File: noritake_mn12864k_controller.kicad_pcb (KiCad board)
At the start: 4 copper layers, 85 x 46.5 mm, 148 parts, among them J1 Conn_01x11, J2 USB_C_Receptacle_USB2.0, J3 TagConnect_TC2030_SWD, J4 Conn_01x18, Q1 AO3400A, Q10 2N7002, Q11 LBSS84LT1G, Q12 2N7002, Q13 TO-252, Q14 CJT04N15, Q15 2N7002, Q16 LBSS84LT1G, Q17 2N7002, Q18 S9015, Q2 AO3400A, Q3 S9015, Q4 AO3401A, Q5 AO3401A, Q6 S9015, Q7 2N7002, Q8 LBSS84LT1G, Q9 2N7002, T1 Wuerth 760390013, T2 Wuerth 760390013, T3 Wuerth 760390013, U1 SN74AVC8T245PW, U10 SRV05-4, U11 SRV05-4, U12 SRV05-4, U2 74HC14, U3 CD4051B, U4 MN12864K, U5 STM32F730R8T6, U6 NE555D, U7 74HC08, U8 SRV05-4, U9 XC6206PxxxMR

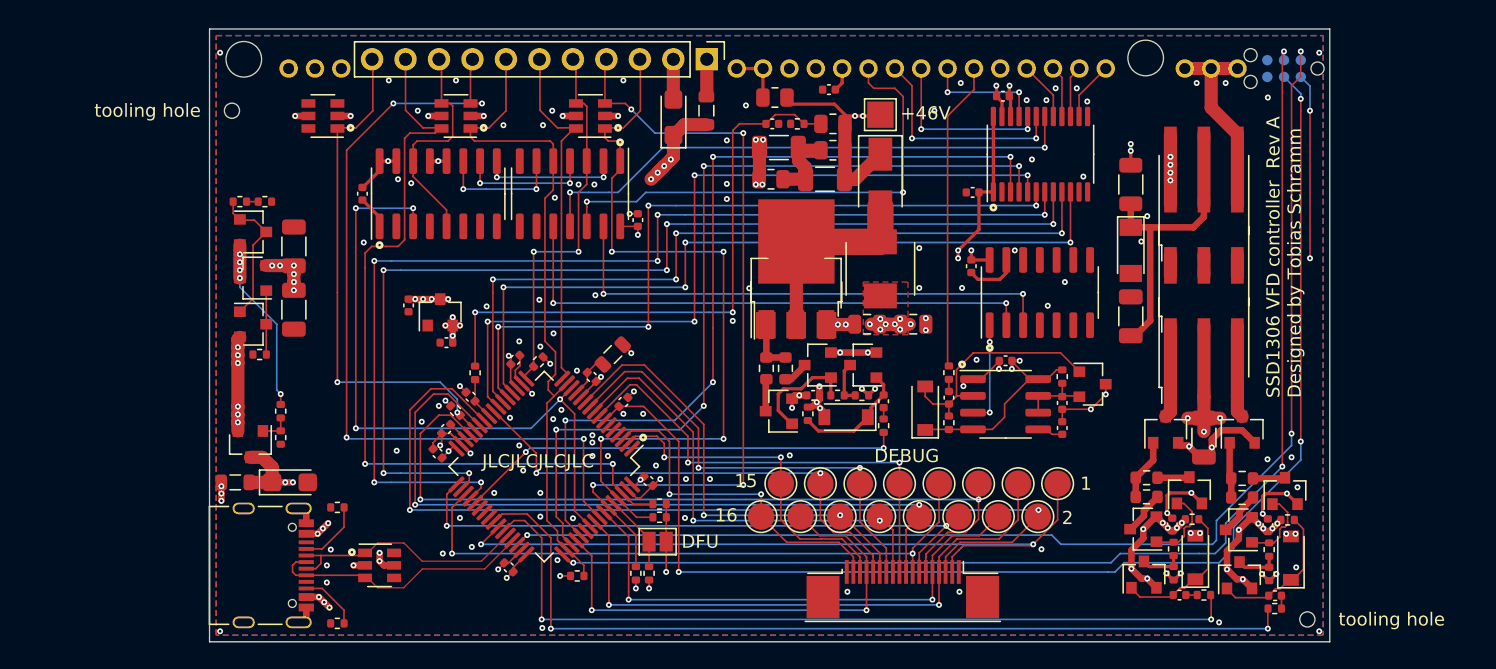
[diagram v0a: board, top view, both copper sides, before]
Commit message: Fix level shifter
Level shifter was flipped in scheatic
Pressed "y" one too many times on that thing :/
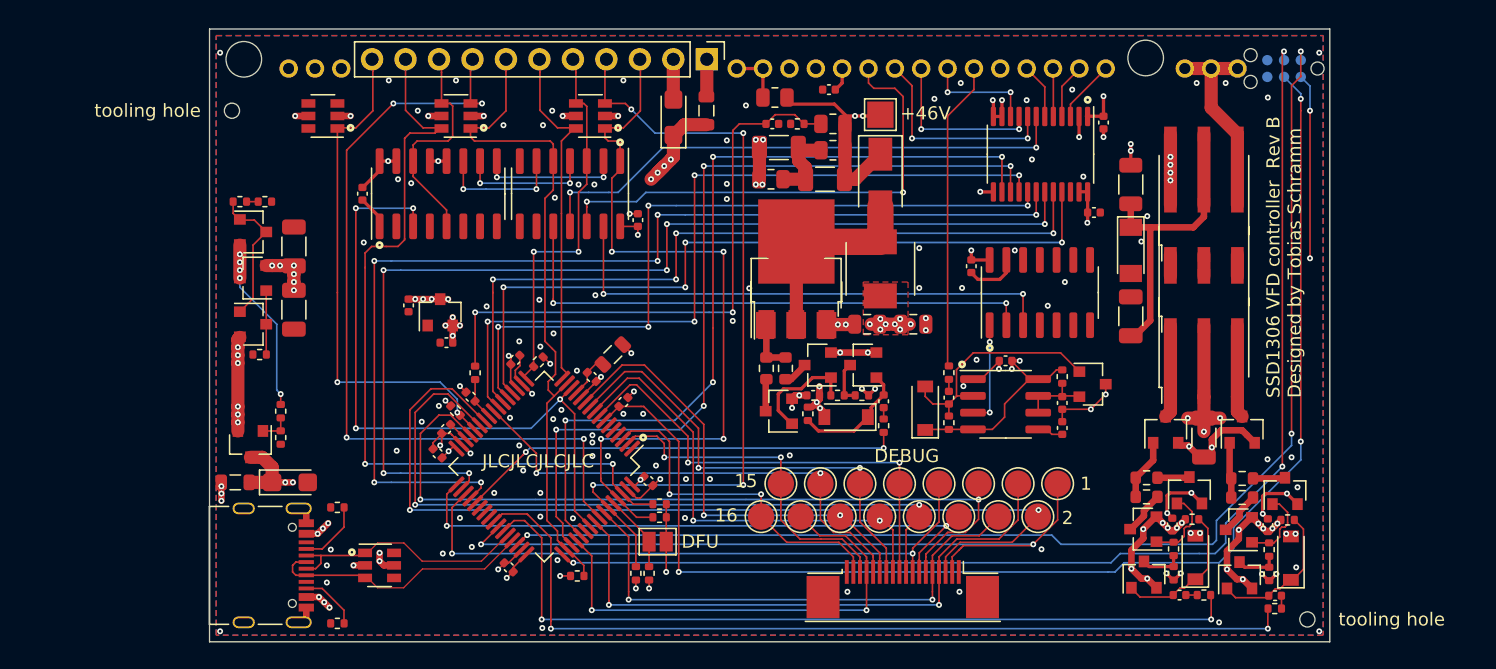
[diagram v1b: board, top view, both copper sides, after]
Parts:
- moved C5 9.33 mm to (167.1, 109.4), turned to 0 degrees
- moved C6 7.89 mm to (167.8, 102.6), turned to 90 degrees
- turned U1 to 270 degrees
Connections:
- U1 pad 1: +3V3 -> +5V
- U1 pad 10: /VFD_BLK -> Net-(U1-Pad10)
- U1 pad 14: Net-(U1-Pad14) -> /VFD_GSIN
- U1 pad 15: Net-(U1-Pad15) -> /VFD_GCLK
- U1 pad 16: Net-(U1-Pad16) -> /VFD_GLAT
- U1 pad 17: Net-(U1-Pad17) -> /VFD_GSBLK
- U1 pad 18: /VFD/sheet60B1BFBD/GBLK_IN -> /VFD_SIN
- U1 pad 19: Net-(U1-Pad19) -> /VFD_CLK
- U1 pad 20: Net-(U1-Pad20) -> /VFD_LAT
- U1 pad 21: Net-(U1-Pad21) -> /VFD_BLK
- U1 pad 23: +5V -> +3V3
- U1 pad 3: /VFD_GSIN -> Net-(U1-Pad3)
- U1 pad 4: /VFD_GCLK -> Net-(U1-Pad4)
- U1 pad 5: /VFD_GLAT -> Net-(U1-Pad5)
- U1 pad 6: /VFD_GSBLK -> Net-(U1-Pad6)
- U1 pad 7: /VFD_SIN -> /VFD/sheet60B1BFBD/GBLK_IN
- U1 pad 8: /VFD_CLK -> Net-(U1-Pad8)
- U1 pad 9: /VFD_LAT -> Net-(U1-Pad9)
- U4 pad 12: Net-(U1-Pad21) -> Net-(U1-Pad10)
- U4 pad 13: Net-(U1-Pad20) -> Net-(U1-Pad9)
- U4 pad 14: Net-(U1-Pad19) -> Net-(U1-Pad8)
- U4 pad 6: Net-(U1-Pad14) -> Net-(U1-Pad3)
- U4 pad 7: Net-(U1-Pad15) -> Net-(U1-Pad4)
- U4 pad 8: Net-(U1-Pad16) -> Net-(U1-Pad5)
- U4 pad 9: Net-(U1-Pad17) -> Net-(U1-Pad6)
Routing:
- net Net-(U1-Pad19): track 17.0 -> 0.00 mm, vias 2 -> 0
- net Net-(U1-Pad8): track 0.00 -> 16.3 mm, vias 0 -> 2
- net Net-(U1-Pad20): track 13.6 -> 0.00 mm, vias 2 -> 0
- net Net-(U1-Pad9): track 0.00 -> 13.0 mm, vias 0 -> 2
- net Net-(U1-Pad21): track 9.06 -> 0.00 mm, vias 2 -> 0
- net Net-(U1-Pad10): track 0.00 -> 8.48 mm, vias 0 -> 2
- net +3V3: track 102.3 -> 93.9 mm, vias 18 -> 17
- net Net-(U1-Pad3): track 0.00 -> 4.76 mm
- net Net-(U1-Pad17): track 4.48 -> 0.00 mm
- net Net-(U1-Pad14): track 4.48 -> 0.00 mm
- net Net-(U1-Pad6): track 0.00 -> 4.22 mm
- net Net-(U1-Pad4): track 0.00 -> 4.13 mm
- net GND: track 84.7 -> 88.8 mm, vias 142 -> 143
- net Net-(U1-Pad16): track 3.92 -> 0.00 mm
- net Net-(U1-Pad15): track 3.92 -> 0.00 mm
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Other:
- board text added: "SSD1306 VFD controller Rev B Designed by Tobias Schramm"
- board text removed: "SSD1306 VFD controller Rev A Designed by Tobias Schramm"

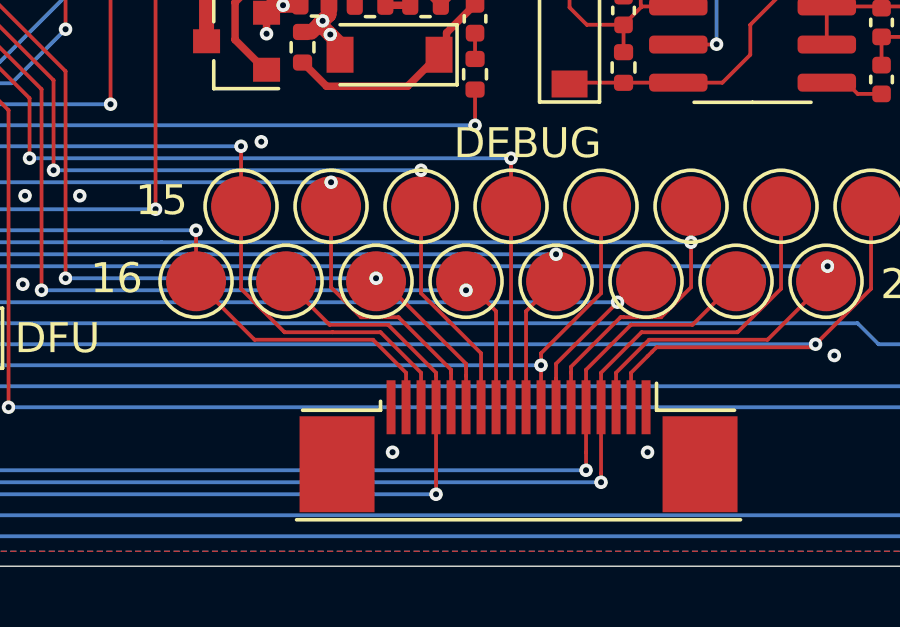
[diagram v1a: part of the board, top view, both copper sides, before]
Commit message: Equalize track spacing on debug connector
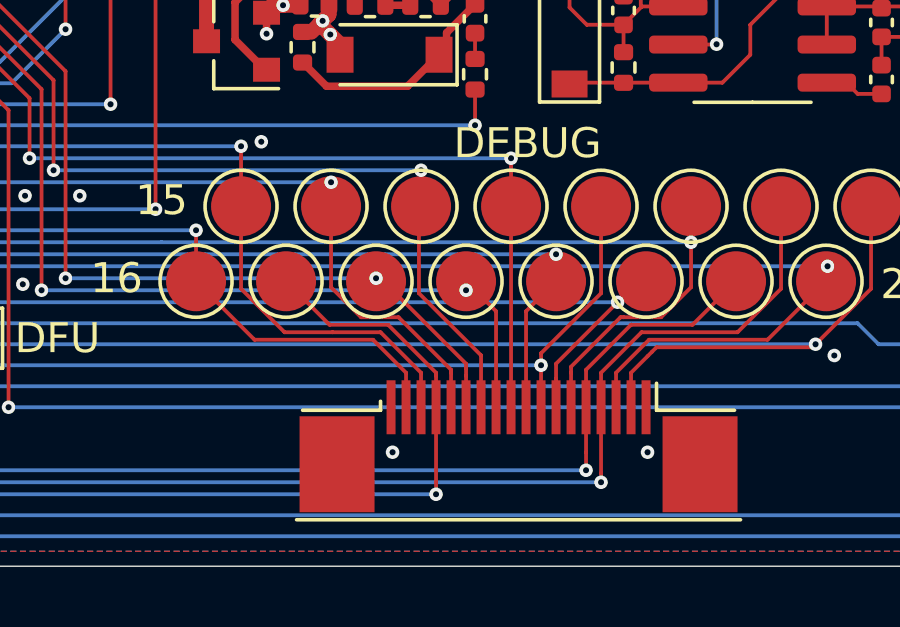
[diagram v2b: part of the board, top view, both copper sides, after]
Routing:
- net /DBG10: track 35.7 -> 35.1 mm

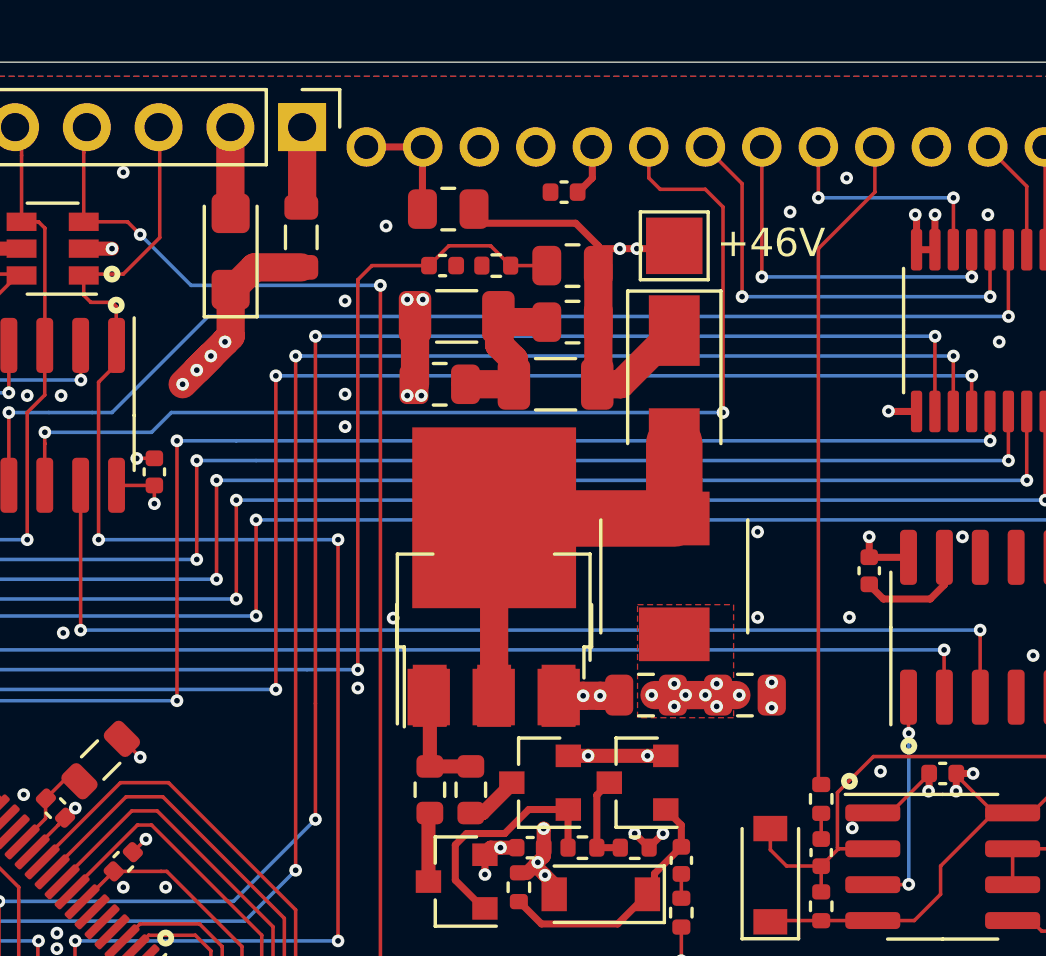
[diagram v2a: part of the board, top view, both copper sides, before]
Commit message: Add additional VFD VDD2 bulk capacitance
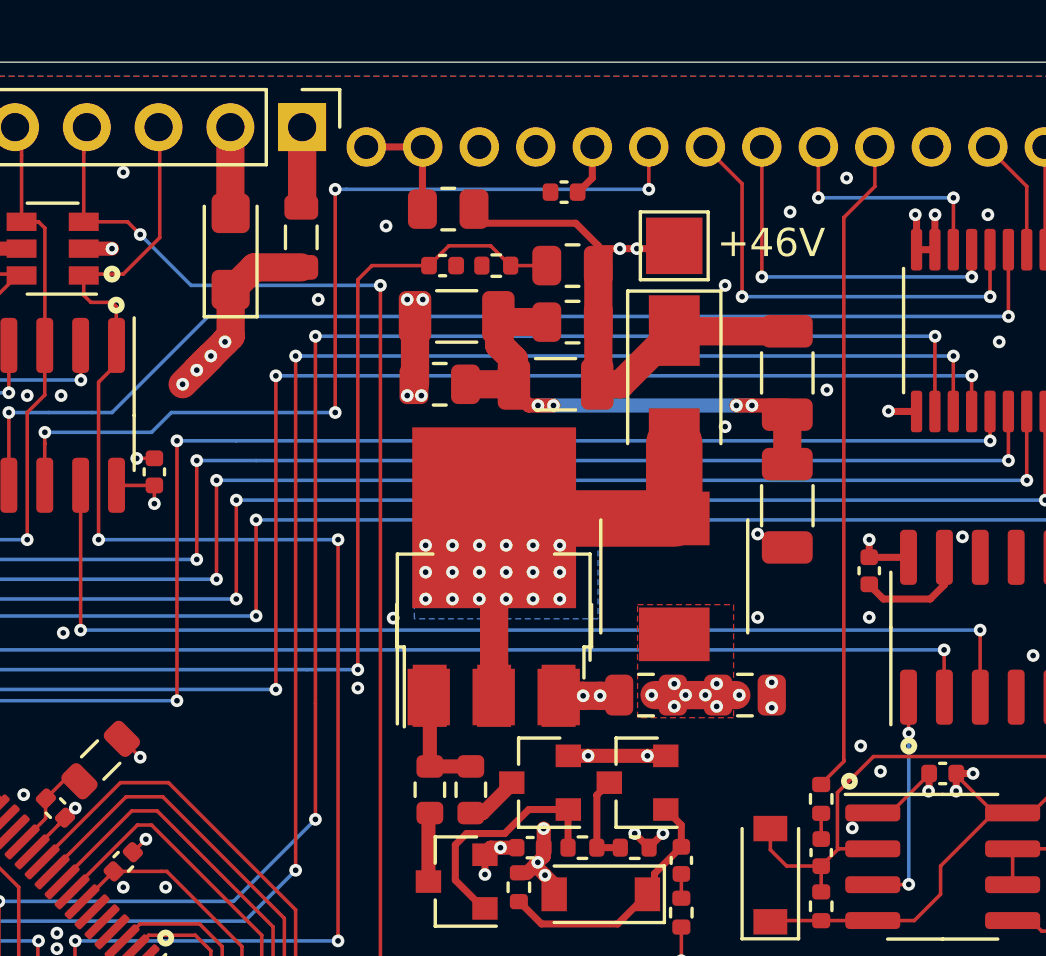
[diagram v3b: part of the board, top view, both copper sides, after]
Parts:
- added C38: 10uF, Capacitor_SMD:C_1206_3216Metric, F.Cu at (154.9, 106.5)
- added C39: 10uF, Capacitor_SMD:C_1206_3216Metric, F.Cu at (154.9, 111.2)
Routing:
- net Net-(C30-Pad2): track 5.89 -> 18.6 mm, vias 0 -> 4
- net /VFD/sheet60B1BFBD/GBLK_OUT: track 37.6 -> 32.9 mm, vias 2 -> 4
- net +48V: track 40.2 -> 44.2 mm
- net Net-(D2-Pad2): vias 0 -> 18
- net GND: vias 143 -> 145
- added copper zone on B.Cu, net Net-(D2-Pad2)
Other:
- net class MV added: clearance 0.25, trace_width 0.09, via_dia 0.45, via_drill 0.2

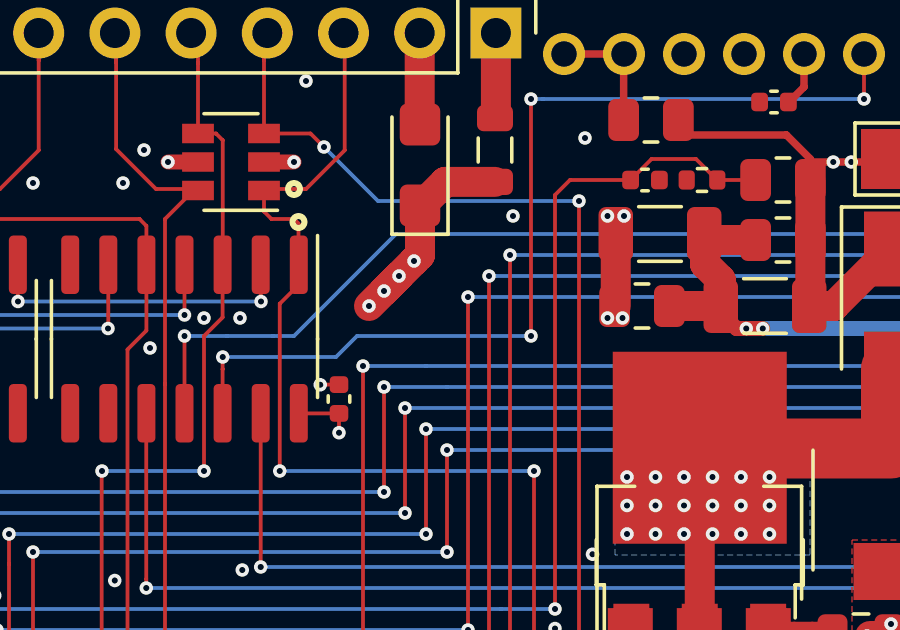
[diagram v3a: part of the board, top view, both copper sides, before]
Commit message: Add additional GND via
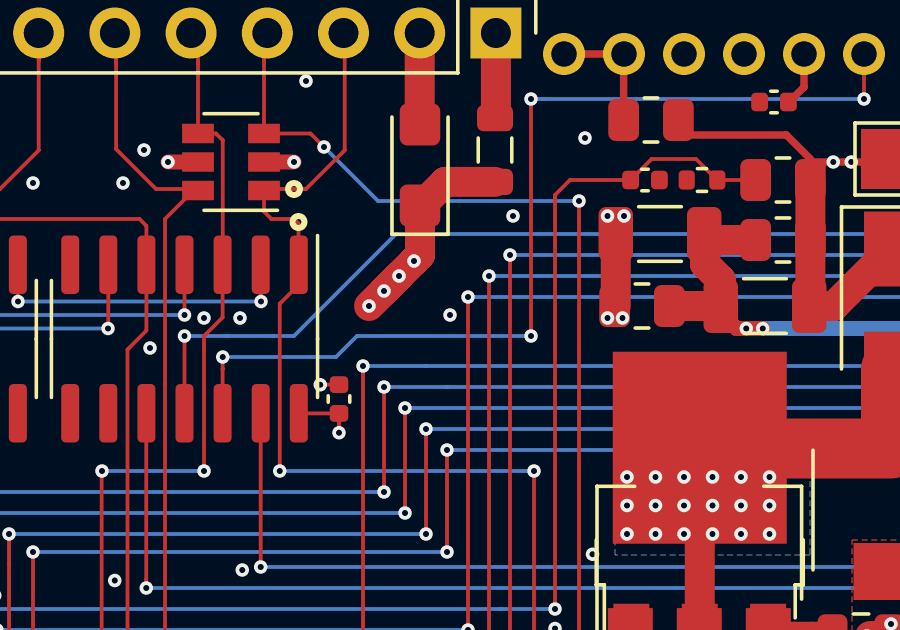
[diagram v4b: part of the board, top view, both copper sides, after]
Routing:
- net GND: vias 145 -> 146
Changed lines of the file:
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@@
     (thickness 1.6)
     (drawings 36)
-    (tracks 1565)
+    (tracks 1566)
     (zones 0)
     (modules 150)
@@
   (via (at 152.7 108.4) (size 0.45) (drill 0.2) (layers F.Cu B.Cu) (net 2))
   (via (at 156.3 107.1) (size 0.45) (drill 0.2) (layers F.Cu B.Cu) (net 2))
+  (via (at 136.2 107.2) (size 0.45) (drill 0.2) (layers F.Cu B.Cu) (net 2))
   (segment (start 157.8 112.4) (end 157.8 113) (width 0.25) (layer F.Cu) (net 3))
   (segment (start 175.45 108.867) (end 175.45 103.475) (width 1) (layer F.Cu) (net 5))
